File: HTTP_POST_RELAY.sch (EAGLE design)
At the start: 28 parts, among them IC1 ATMEGA328V-10P, IC2 7805T, IC3 ULN2003AN, Q1 16M

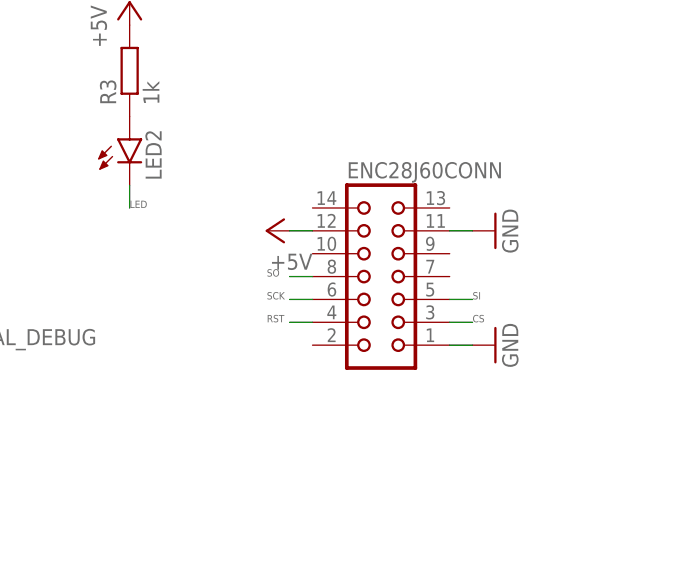
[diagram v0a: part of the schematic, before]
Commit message: add microcontroller firmware
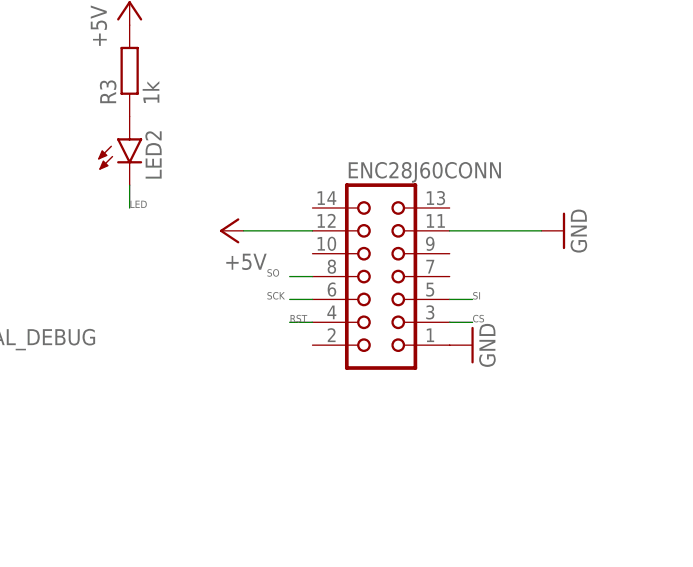
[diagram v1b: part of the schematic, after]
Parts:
- Q1: device crystal:CRYSTALHC49S -> crystal:CRYSTALHC49U-V
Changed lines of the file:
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@@
 <part name="P+6" library="supply1" library_urn="urn:adsk.eagle:library:371" deviceset="+5V" device=""/>
 <part name="GND6" library="supply1" library_urn="urn:adsk.eagle:library:371" deviceset="GND" device=""/>
-<part name="Q1" library="crystal" library_urn="urn:adsk.eagle:library:204" deviceset="CRYSTAL" device="HC49S" package3d_urn="urn:adsk.eagle:package:12071/1" value="16M"/>
+<part name="Q1" library="crystal" deviceset="CRYSTAL" device="HC49U-V" package3d_urn="urn:adsk.eagle:package:12075/1" value="16M"/>
 <part name="C5" library="rcl-nelson" deviceset="C-EU" device="025-024X044" package3d_urn="urn:adsk.eagle:package:23630/1" value="22p"/>
 <part name="C6" library="rcl-nelson" deviceset="C-EU" device="025-024X044" package3d_urn="urn:adsk.eagle:package:23630/1" value="22p"/>
@@
 <part name="P+8" library="supply1" library_urn="urn:adsk.eagle:library:371" deviceset="+5V" device=""/>
 <part name="ENC28J60CONN" library="con-harting-nelson" deviceset="CON14" device="" package3d_urn="urn:adsk.eagle:package:7117/1"/>
-<part name="GND10" library="supply1" library_urn="urn:adsk.eagle:library:371" deviceset="GND" device=""/>
 <part name="P+9" library="supply1" library_urn="urn:adsk.eagle:library:371" deviceset="+5V" device=""/>
 <part name="GND11" library="supply1" library_urn="urn:adsk.eagle:library:371" deviceset="GND" device=""/>
 <part name="SERIAL_DEBUG" library="con-amp" library_urn="urn:adsk.eagle:library:127" deviceset="MTA03-100" device="" package3d_urn="urn:adsk.eagle:package:8081621/1"/>
 <part name="GND12" library="supply1" library_urn="urn:adsk.eagle:library:371" deviceset="GND" device=""/>
-<part name="LED2" library="led" library_urn="urn:adsk.eagle:library:259" deviceset="LED" device="5MM" package3d_urn="urn:adsk.eagle:package:15799/2"/>
+<part name="LED2" library="led" deviceset="LED" device="5MM" package3d_urn="urn:adsk.eagle:package:15799/2"/>
 <part name="R3" library="rcl-nelson" deviceset="R-EU_" device="0204/7" package3d_urn="urn:adsk.eagle:package:23498/2" value="1k"/>
 <part name="P+10" library="supply1" library_urn="urn:adsk.eagle:library:371" deviceset="+5V" device=""/>
@@
 <part name="R5" library="rcl-nelson" deviceset="R-EU_" device="0204/7" package3d_urn="urn:adsk.eagle:package:23498/2" value="10k"/>
 <part name="INS" library="con-ptr500" library_urn="urn:adsk.eagle:library:181" deviceset="AK300/3" device="" package3d_urn="urn:adsk.eagle:package:9878/1"/>
+<part name="GND10" library="supply1" library_urn="urn:adsk.eagle:library:371" deviceset="GND" device=""/>
 </parts>
 <sheets>
@@
 <attribute name="NAME" x="163.83" y="79.502" size="1.778" layer="95"/>
 </instance>
-<instance part="GND10" gate="1" x="180.34" y="60.96" smashed="yes" rot="R90">
-<attribute name="VALUE" x="182.88" y="58.42" size="1.778" layer="96" rot="R90"/>
-</instance>
-<instance part="P+9" gate="1" x="154.94" y="73.66" smashed="yes" rot="R90">
-<attribute name="VALUE" x="160.02" y="71.12" size="1.778" layer="96" rot="R180"/>
-</instance>
-<instance part="GND11" gate="1" x="180.34" y="73.66" smashed="yes" rot="R90">
-<attribute name="VALUE" x="182.88" y="71.12" size="1.778" layer="96" rot="R90"/>
+<instance part="P+9" gate="1" x="149.86" y="73.66" smashed="yes" rot="R90">
+<attribute name="VALUE" x="154.94" y="71.12" size="1.778" layer="96" rot="R180"/>
+</instance>
+<instance part="GND11" gate="1" x="187.96" y="73.66" smashed="yes" rot="R90">
+<attribute name="VALUE" x="190.5" y="71.12" size="1.778" layer="96" rot="R90"/>
 </instance>
 <instance part="SERIAL_DEBUG" gate="G$1" x="114.3" y="60.96" smashed="yes">
@@
 <attribute name="NAME" x="36.83" y="-14.351" size="1.778" layer="95" rot="R180"/>
 <attribute name="VALUE" x="34.29" y="-18.923" size="1.778" layer="96"/>
+</instance>
+<instance part="GND10" gate="1" x="177.8" y="60.96" smashed="yes" rot="R90">
+<attribute name="VALUE" x="180.34" y="58.42" size="1.778" layer="96" rot="R90"/>
 </instance>
 </instances>
@@
 </segment>
 <segment>
-<pinref part="ENC28J60CONN" gate="G$1" pin="12"/>
-<pinref part="P+9" gate="1" pin="+5V"/>
-<wire x1="157.48" y1="73.66" x2="160.02" y2="73.66" width="0.1524" layer="91"/>
-</segment>
-<segment>
 <pinref part="R3" gate="G$1" pin="2"/>
 <pinref part="P+10" gate="1" pin="+5V"/>
@@
 <pinref part="P+12" gate="1" pin="+5V"/>
 <wire x1="111.76" y1="-17.78" x2="109.22" y2="-17.78" width="0.1524" layer="91"/>
+</segment>
+<segment>
+<pinref part="ENC28J60CONN" gate="G$1" pin="12"/>
+<pinref part="P+9" gate="1" pin="+5V"/>
+<wire x1="152.4" y1="73.66" x2="160.02" y2="73.66" width="0.1524" layer="91"/>
 </segment>
 </net>
@@
 </segment>
 <segment>
+<pinref part="SERIAL_DEBUG" gate="G$1" pin="1"/>
+<pinref part="GND12" gate="1" pin="GND"/>
+</segment>
+<segment>
+<pinref part="IC3" gate="A" pin="GND"/>
+<pinref part="GND13" gate="1" pin="GND"/>
+</segment>
+<segment>
+<pinref part="INS" gate="-3" pin="KL"/>
+<pinref part="GND14" gate="1" pin="GND"/>
+</segment>
+<segment>
+<pinref part="ENC28J60CONN" gate="G$1" pin="11"/>
+<pinref part="GND11" gate="1" pin="GND"/>
+<wire x1="185.42" y1="73.66" x2="175.26" y2="73.66" width="0.1524" layer="91"/>
+</segment>
+<segment>
 <pinref part="ENC28J60CONN" gate="G$1" pin="1"/>
 <pinref part="GND10" gate="1" pin="GND"/>
-<wire x1="177.8" y1="60.96" x2="175.26" y2="60.96" width="0.1524" layer="91"/>
-</segment>
-<segment>
-<pinref part="ENC28J60CONN" gate="G$1" pin="11"/>
-<pinref part="GND11" gate="1" pin="GND"/>
-<wire x1="177.8" y1="73.66" x2="175.26" y2="73.66" width="0.1524" layer="91"/>
-</segment>
-<segment>
-<pinref part="SERIAL_DEBUG" gate="G$1" pin="1"/>
-<pinref part="GND12" gate="1" pin="GND"/>
-</segment>
-<segment>
-<pinref part="IC3" gate="A" pin="GND"/>
-<pinref part="GND13" gate="1" pin="GND"/>
-</segment>
-<segment>
-<pinref part="INS" gate="-3" pin="KL"/>
-<pinref part="GND14" gate="1" pin="GND"/>
 </segment>
 </net>
@@
 <net name="SI" class="0">
 <segment>
+<pinref part="IC1" gate="G$1" pin="(PCI3/MOSI/OC2A)PB3"/>
+<wire x1="101.6" y1="22.86" x2="104.14" y2="22.86" width="0.1524" layer="91"/>
+<label x="104.14" y="22.86" size="0.8128" layer="95"/>
+</segment>
+<segment>
 <pinref part="ENC28J60CONN" gate="G$1" pin="5"/>
 <wire x1="175.26" y1="66.04" x2="177.8" y2="66.04" width="0.1524" layer="91"/>
 <label x="177.8" y="66.04" size="0.8128" layer="95"/>
 </segment>
-<segment>
-<pinref part="IC1" gate="G$1" pin="(PCI3/MOSI/OC2A)PB3"/>
-<wire x1="101.6" y1="22.86" x2="104.14" y2="22.86" width="0.1524" layer="91"/>
-<label x="104.14" y="22.86" size="0.8128" layer="95"/>
-</segment>
 </net>
 <net name="SCK" class="0">
+<segment>
+<pinref part="IC1" gate="G$1" pin="(PCI5/SCK)PB5"/>
+<wire x1="101.6" y1="17.78" x2="104.14" y2="17.78" width="0.1524" layer="91"/>
+<label x="104.14" y="17.78" size="0.8128" layer="95"/>
+</segment>
 <segment>
 <pinref part="ENC28J60CONN" gate="G$1" pin="6"/>
@@
 <label x="154.94" y="66.04" size="0.8128" layer="95"/>
 </segment>
-<segment>
-<pinref part="IC1" gate="G$1" pin="(PCI5/SCK)PB5"/>
-<wire x1="101.6" y1="17.78" x2="104.14" y2="17.78" width="0.1524" layer="91"/>
-<label x="104.14" y="17.78" size="0.8128" layer="95"/>
-</segment>
 </net>
 <net name="SO" class="0">
+<segment>
+<pinref part="IC1" gate="G$1" pin="(PCI4/MISO)PB4"/>
+<wire x1="101.6" y1="20.32" x2="104.14" y2="20.32" width="0.1524" layer="91"/>
+<label x="104.14" y="20.32" size="0.8128" layer="95"/>
+</segment>
 <segment>
 <pinref part="ENC28J60CONN" gate="G$1" pin="8"/>
@@
 <label x="154.94" y="68.58" size="0.8128" layer="95"/>
 </segment>
-<segment>
-<pinref part="IC1" gate="G$1" pin="(PCI4/MISO)PB4"/>
-<wire x1="101.6" y1="20.32" x2="104.14" y2="20.32" width="0.1524" layer="91"/>
-<label x="104.14" y="20.32" size="0.8128" layer="95"/>
-</segment>
 </net>
 <net name="RST" class="0">
-<segment>
-<pinref part="ENC28J60CONN" gate="G$1" pin="4"/>
-<wire x1="160.02" y1="63.5" x2="157.48" y2="63.5" width="0.1524" layer="91"/>
-<label x="154.94" y="63.5" size="0.8128" layer="95"/>
-</segment>
 <segment>
 <pinref part="IC3" gate="A" pin="O5"/>
@@
 <label x="88.9" y="-20.32" size="0.8128" layer="95"/>
 </segment>
-</net>
+<segment>
+<pinref part="ENC28J60CONN" gate="G$1" pin="4"/>
+<wire x1="160.02" y1="63.5" x2="157.48" y2="63.5" width="0.1524" layer="91"/>
+<label x="157.48" y="63.5" size="0.8128" layer="95"/>
+</segment>
+</net>
